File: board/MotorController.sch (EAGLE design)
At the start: 34 parts, among them Q1 IPP80P03P4L-04, Q2 8Mhz, T1 BT139X-600E, U1 ATTINY84-20PU

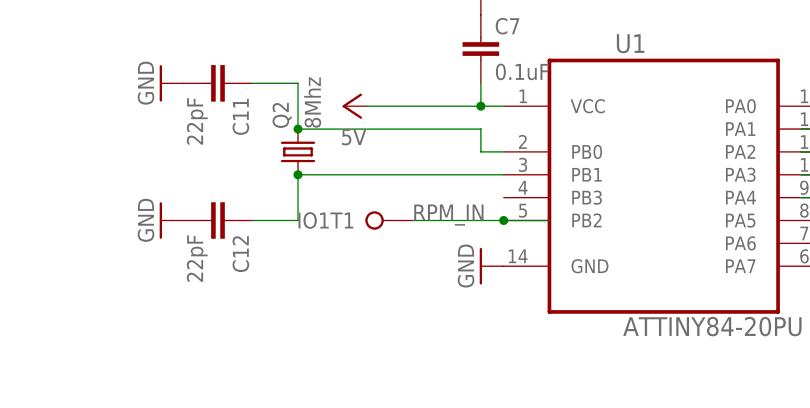
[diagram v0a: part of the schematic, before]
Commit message: Pull up reset line
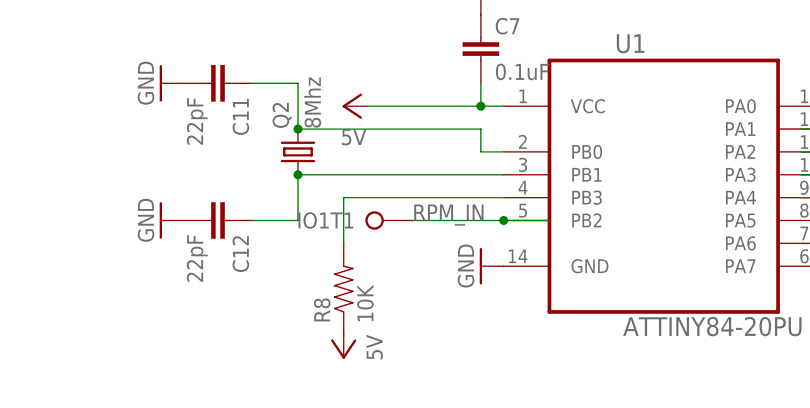
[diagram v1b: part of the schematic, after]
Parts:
- added R8: 10K, SaintGimp:RESISTOR-7.5MM
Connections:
- new net N$2: R8.2, U1.PB3
- new net VCC: R8.1
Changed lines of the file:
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@@
 <part name="5V1" library="SaintGimp" deviceset="VCC" device="" value="5V"/>
 <part name="5V2" library="SaintGimp" deviceset="VCC" device="" value="5V"/>
+<part name="R8" library="SaintGimp" deviceset="RESISTOR-*" device="7.5MM" value="10K"/>
+<part name="5V3" library="SaintGimp" deviceset="VCC" device="" value="5V"/>
 </parts>
 <sheets>
@@
 <instance part="5V1" gate="VCC" x="167.64" y="10.16"/>
 <instance part="5V2" gate="VCC" x="167.64" y="-20.32" rot="R180"/>
+<instance part="R8" gate="G$1" x="83.82" y="-12.7" rot="R90"/>
+<instance part="5V3" gate="VCC" x="83.82" y="-20.32" rot="R180"/>
 </instances>
 <busses>
@@
 </segment>
 </net>
+<net name="N$2" class="0">
+<segment>
+<pinref part="U1" gate="A" pin="PB3"/>
+<wire x1="101.6" y1="-2.54" x2="83.82" y2="-2.54" width="0.1524" layer="91"/>
+<wire x1="83.82" y1="-2.54" x2="83.82" y2="-7.62" width="0.1524" layer="91"/>
+<pinref part="R8" gate="G$1" pin="2"/>
+</segment>
+</net>
+<net name="VCC" class="0">
+<segment>
+<pinref part="R8" gate="G$1" pin="1"/>
+<pinref part="5V3" gate="VCC" pin="VCC"/>
+</segment>
+</net>

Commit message: New board layout
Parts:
- removed 5VDISP, 5VPOT: SCREW-TERM-2, SaintGimp:SCREW-TERM-2
- removed IO1, IO2, IO3: SCREW-TERM-3, SaintGimp:SCREW-TERM-3
- removed R7: 2.2K, SaintGimp:RESISTOR-7.5MM
- added C10: 0.1uF, SaintGimp:CAPACITOR-5MM
- added CNTRL: SCREW-TERM-2, SaintGimp:SCREW-TERM-2
- added DISP, MOTOR, RAMP, SPD: SCREW-TERM-3, SaintGimp:SCREW-TERM-3
- C11, C12: device SaintGimp:CAPACITOR-5MM -> SaintGimp:CAPACITOR-2.5MM
- C6: value 0.1uF -> 1uF
- F1: value FUSEBLANK_5X20MM -> 4A
- R1, R2: value 1K -> (none)
- R3, R8: value 10K -> (none)
- R4, R5: value 220 -> (none)
- R6: value 2.2K -> (none)
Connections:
- removed net 5V: 5VDISPT1.KL, 5VPOTT1.KL, C2.+, C3.1, C7.2, DC1.OUT, R6.2, R7.1, U1.VCC
- removed net I2C_SCL: IO2T2.KL, R6.1, U1.PA4
- removed net I2C_SDA: IO1T3.KL, R7.2, U1.PA6
- new net N$8: DISPT3.KL, R6.1
- new net SERIAL_TX: R6.2, U1.PA6
- net 24V-PROTECTED: now also C10.2
- net DIR_IN: now also CNTRLT1.KL; no longer IO3T1.KL
- net DIR_OUT: now also MOTORT3.KL; no longer IO1T2.KL
- net GND: now also C10.1, DISPT2.KL, RAMPT2.KL, SPDT2.KL; no longer 5VDISPT2.KL, 5VPOTT2.KL
- net N$10: now also MOTORT1.KL; no longer IO2T1.KL
- net RAMP_IN: now also RAMPT3.KL; no longer IO3T2.KL
- net RPM_IN: now also MOTORT2.KL; no longer IO1T1.KL
- net SPD_IN: now also SPDT3.KL; no longer IO3T3.KL
- net START_IN: now also CNTRLT2.KL; no longer IO2T3.KL
- net VCC: now also C2.+, C3.1, C7.2, DC1.OUT, DISPT1.KL, RAMPT1.KL, SPDT1.KL, U1.VCC
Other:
- moved on the sheet: 24VOUTT1, 24VOUTT2, C11, C12, C2, C3, C4, C6, C7, C8, C9, DC1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

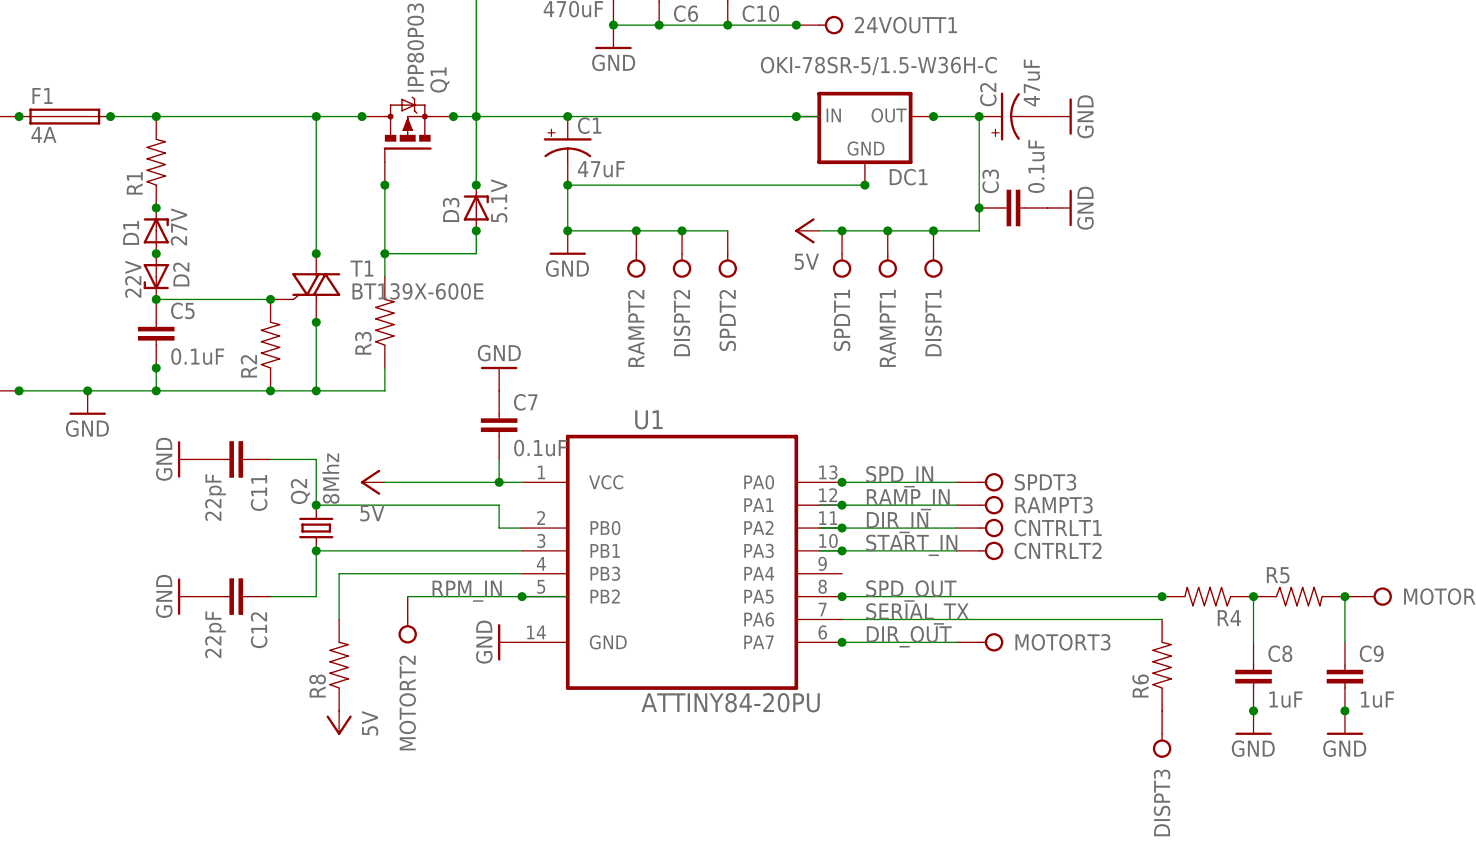
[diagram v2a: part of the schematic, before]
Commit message: Restore resistor values
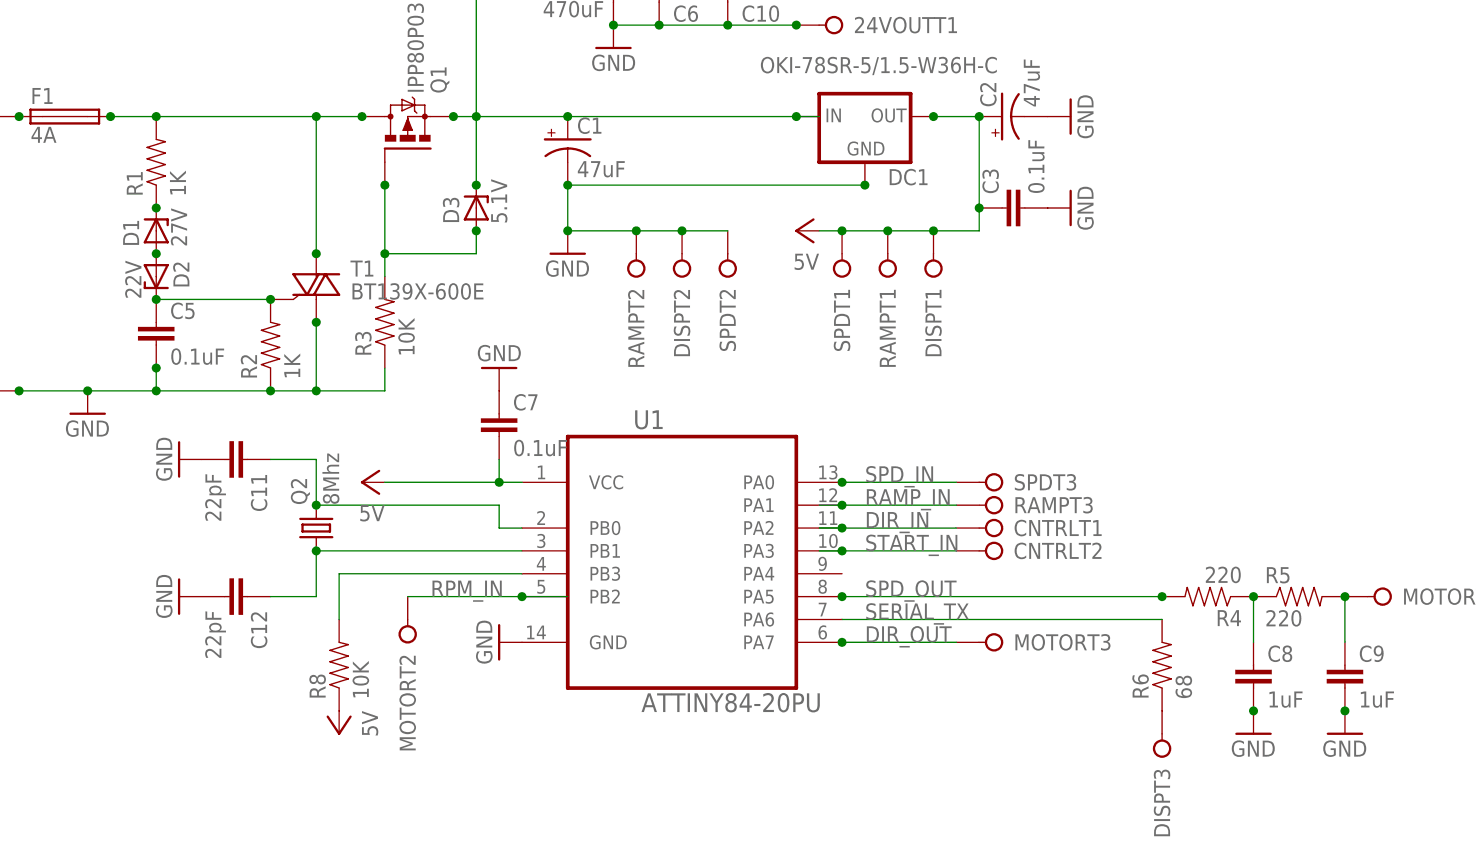
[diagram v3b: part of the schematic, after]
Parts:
- R1, R2: value (none) -> 1K
- R3, R8: value (none) -> 10K
- R4, R5: value (none) -> 220
- R6: value (none) -> 68
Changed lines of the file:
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@@
 <part name="D2" library="SaintGimp" deviceset="ZENER" device="-7.5" value="22V"/>
 <part name="D1" library="SaintGimp" deviceset="ZENER" device="-7.5" value="27V"/>
-<part name="R1" library="SaintGimp" deviceset="RESISTOR-*" device="7.5MM"/>
+<part name="R1" library="SaintGimp" deviceset="RESISTOR-*" device="7.5MM" value="1K"/>
 <part name="C5" library="SaintGimp" deviceset="CAPACITOR-*" device="5MM" value="0.1uF"/>
-<part name="R2" library="SaintGimp" deviceset="RESISTOR-*" device="7.5MM"/>
+<part name="R2" library="SaintGimp" deviceset="RESISTOR-*" device="7.5MM" value="1K"/>
 <part name="Q1" library="SaintGimp" deviceset="IPP80P03P4L-04" device="-H" value="IPP80P03P4L-04"/>
-<part name="R3" library="SaintGimp" deviceset="RESISTOR-*" device="7.5MM"/>
+<part name="R3" library="SaintGimp" deviceset="RESISTOR-*" device="7.5MM" value="10K"/>
 <part name="D3" library="SaintGimp" deviceset="ZENER" device="-7.5" value="5.1V"/>
 <part name="C2" library="SaintGimp" deviceset="CAP-POL" device="-2.5-5" value="47uF"/>
@@
 <part name="U1" library="SaintGimp" deviceset="ATTINY84-20PU" device=""/>
 <part name="C7" library="SaintGimp" deviceset="CAPACITOR-*" device="5MM" value="0.1uF"/>
-<part name="R4" library="SaintGimp" deviceset="RESISTOR-*" device="7.5MM"/>
-<part name="R5" library="SaintGimp" deviceset="RESISTOR-*" device="7.5MM"/>
+<part name="R4" library="SaintGimp" deviceset="RESISTOR-*" device="7.5MM" value="220"/>
+<part name="R5" library="SaintGimp" deviceset="RESISTOR-*" device="7.5MM" value="220"/>
 <part name="C8" library="SaintGimp" deviceset="CAPACITOR-*" device="5MM" value="1uF"/>
 <part name="GND7" library="SaintGimp" deviceset="GND" device=""/>
@@
 <part name="5V1" library="SaintGimp" deviceset="VCC" device="" value="5V"/>
 <part name="DC1" library="SaintGimp" deviceset="DC-CONV" device="" value="OKI-78SR-5/1.5-W36H-C"/>
-<part name="R8" library="SaintGimp" deviceset="RESISTOR-*" device="7.5MM"/>
+<part name="R8" library="SaintGimp" deviceset="RESISTOR-*" device="7.5MM" value="10K"/>
 <part name="5V3" library="SaintGimp" deviceset="VCC" device="" value="5V"/>
 <part name="C10" library="SaintGimp" deviceset="CAPACITOR-*" device="5MM" value="0.1uF"/>
-<part name="R6" library="SaintGimp" deviceset="RESISTOR-*" device="7.5MM"/>
+<part name="R6" library="SaintGimp" deviceset="RESISTOR-*" device="7.5MM" value="68"/>
 <part name="SPD" library="SaintGimp" deviceset="SCREW-TERM-3" device=""/>
 <part name="MOTOR" library="SaintGimp" deviceset="SCREW-TERM-3" device=""/>

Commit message: Board tweaks
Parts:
- removed C2: 47uF, SaintGimp:CAP-POL-2.5-5
- removed CNTRL: SCREW-TERM-2, SaintGimp:SCREW-TERM-2
- removed DISP, SPD: SCREW-TERM-3, SaintGimp:SCREW-TERM-3
- added FRONT: SCREW-TERM-5, SaintGimp:SCREW-TERM-5
- added MODE: SCREW-TERM-2, SaintGimp:SCREW-TERM-2
- C1: value 47uF -> 10uF; device SaintGimp:CAP-POL-2.5-5 -> SaintGimp:CAPACITOR-5MM
- C3: value 0.1uF -> 10uF
- MOTOR: value SCREW-TERM-3 -> SCREW-TERM-4; device SaintGimp:SCREW-TERM-3 -> SaintGimp:SCREW-TERM-4
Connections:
- net 24V-PROTECTED: now also C1.1; no longer C1.+
- net DIR_IN: now also MODET2.KL; no longer CNTRLT1.KL
- net GND: now also C1.2, FRONTT2.KL, MODET1.KL, MOTORT4.KL; no longer C1.-, C2.-, DISPT2.KL, SPDT2.KL
- net N$8: now also FRONTT3.KL; no longer DISPT3.KL
- net SPD_IN: now also FRONTT4.KL; no longer SPDT3.KL
- net START_IN: now also FRONTT5.KL; no longer CNTRLT2.KL
- net VCC: now also FRONTT1.KL; no longer C2.+, DISPT1.KL, SPDT1.KL
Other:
- moved on the sheet: C3
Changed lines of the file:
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@@
 <part name="24VOUT" library="SaintGimp" deviceset="SCREW-TERM-2" device=""/>
 <part name="RAMP" library="SaintGimp" deviceset="SCREW-TERM-3" device=""/>
-<part name="DISP" library="SaintGimp" deviceset="SCREW-TERM-3" device=""/>
-<part name="C1" library="SaintGimp" deviceset="CAP-POL" device="-2.5-5" value="47uF"/>
+<part name="FRONT" library="SaintGimp" deviceset="SCREW-TERM-5" device=""/>
 <part name="C4" library="SaintGimp" deviceset="CAP-POL" device="-25-14" value="470uF"/>
 <part name="F1" library="SaintGimp" deviceset="FUSE" device="" value="4A"/>
@@
 <part name="R3" library="SaintGimp" deviceset="RESISTOR-*" device="7.5MM" value="10K"/>
 <part name="D3" library="SaintGimp" deviceset="ZENER" device="-7.5" value="5.1V"/>
-<part name="C2" library="SaintGimp" deviceset="CAP-POL" device="-2.5-5" value="47uF"/>
-<part name="GND2" library="SaintGimp" deviceset="GND" device=""/>
-<part name="C3" library="SaintGimp" deviceset="CAPACITOR-*" device="5MM" value="0.1uF"/>
+<part name="C3" library="SaintGimp" deviceset="CAPACITOR-*" device="5MM" value="10uF"/>
 <part name="GND3" library="SaintGimp" deviceset="GND" device=""/>
 <part name="C6" library="SaintGimp" deviceset="CAPACITOR-*" device="5MM" value="1uF"/>
@@
 <part name="C10" library="SaintGimp" deviceset="CAPACITOR-*" device="5MM" value="0.1uF"/>
 <part name="R6" library="SaintGimp" deviceset="RESISTOR-*" device="7.5MM" value="68"/>
-<part name="SPD" library="SaintGimp" deviceset="SCREW-TERM-3" device=""/>
-<part name="MOTOR" library="SaintGimp" deviceset="SCREW-TERM-3" device=""/>
-<part name="CNTRL" library="SaintGimp" deviceset="SCREW-TERM-2" device=""/>
+<part name="MOTOR" library="SaintGimp" deviceset="SCREW-TERM-4" device=""/>
+<part name="MODE" library="SaintGimp" deviceset="SCREW-TERM-2" device=""/>
+<part name="C1" library="SaintGimp" deviceset="CAPACITOR-*" device="5MM" value="10uF"/>
 </parts>
 <sheets>
@@
 <instance part="RAMP" gate="T1" x="76.2" y="35.56" rot="R90"/>
 <instance part="RAMP" gate="T2" x="48.26" y="35.56" rot="R90"/>
-<instance part="DISP" gate="T1" x="81.28" y="35.56" rot="R90"/>
-<instance part="DISP" gate="T2" x="53.34" y="35.56" rot="R90"/>
-<instance part="C1" gate="G$1" x="40.64" y="50.8"/>
+<instance part="FRONT" gate="T1" x="81.28" y="35.56" rot="R90"/>
+<instance part="FRONT" gate="T2" x="53.34" y="35.56" rot="R90"/>
 <instance part="C4" gate="G$1" x="45.72" y="68.58" rot="MR0"/>
 <instance part="F1" gate="G$1" x="-15.24" y="53.34"/>
@@
 <instance part="R3" gate="G$1" x="20.32" y="30.48" rot="R90"/>
 <instance part="D3" gate="G$1" x="30.48" y="43.18" rot="R90"/>
-<instance part="C2" gate="G$1" x="88.9" y="53.34" rot="R90"/>
-<instance part="GND2" gate="1" x="96.52" y="53.34" rot="R90"/>
-<instance part="C3" gate="G$1" x="91.44" y="43.18" rot="R90"/>
-<instance part="GND3" gate="1" x="96.52" y="43.18" rot="R90"/>
+<instance part="C3" gate="G$1" x="91.44" y="48.26" rot="R90"/>
+<instance part="GND3" gate="1" x="96.52" y="48.26" rot="R90"/>
 <instance part="C6" gate="G$1" x="50.8" y="68.58" rot="MR180"/>
 <instance part="GND6" gate="1" x="33.02" y="-5.08" rot="R270"/>
@@
 <instance part="GND12" gate="1" x="-2.54" y="0" rot="R270"/>
 <instance part="5V2" gate="VCC" x="17.78" y="12.7" rot="R90"/>
-<instance part="5V1" gate="VCC" x="66.04" y="40.64" rot="R90"/>
+<instance part="5V1" gate="VCC" x="71.12" y="40.64" rot="R90"/>
 <instance part="DC1" gate="G$1" x="73.66" y="50.8" smashed="yes">
 <attribute name="NAME" x="76.2" y="45.72" size="1.778" layer="95"/>
@@
 <instance part="C10" gate="G$1" x="58.42" y="68.58" rot="MR180"/>
 <instance part="R6" gate="G$1" x="106.68" y="-7.62" rot="R90"/>
-<instance part="DISP" gate="T3" x="106.68" y="-17.78" rot="R90"/>
-<instance part="SPD" gate="T3" x="88.9" y="12.7" rot="R180"/>
-<instance part="SPD" gate="T1" x="71.12" y="35.56" rot="R90"/>
-<instance part="SPD" gate="T2" x="58.42" y="35.56" rot="R90"/>
+<instance part="FRONT" gate="T3" x="106.68" y="-17.78" rot="R90"/>
 <instance part="RAMP" gate="T3" x="88.9" y="10.16" rot="R180"/>
 <instance part="MOTOR" gate="T1" x="132.08" y="0" rot="R180"/>
-<instance part="CNTRL" gate="T2" x="88.9" y="5.08" rot="R180"/>
-<instance part="CNTRL" gate="T1" x="88.9" y="7.62" rot="R180"/>
 <instance part="MOTOR" gate="T2" x="22.86" y="-5.08" rot="R90"/>
 <instance part="MOTOR" gate="T3" x="88.9" y="-5.08" rot="R180"/>
+<instance part="FRONT" gate="T4" x="88.9" y="12.7" rot="R180"/>
+<instance part="FRONT" gate="T5" x="88.9" y="5.08" rot="R180"/>
+<instance part="MODE" gate="T2" x="88.9" y="7.62" rot="R180"/>
+<instance part="MODE" gate="T1" x="58.42" y="35.56" rot="R90"/>
+<instance part="MOTOR" gate="T4" x="63.5" y="35.56" rot="R90"/>
+<instance part="C1" gate="G$1" x="40.64" y="48.26"/>
 </instances>
 <busses>
@@
 <net name="GND" class="0">
 <segment>
-<pinref part="C1" gate="G$1" pin="-"/>
 <pinref part="GND1" gate="1" pin="GND"/>
 <wire x1="40.64" y1="40.64" x2="40.64" y2="45.72" width="0.1524" layer="91"/>
 <wire x1="73.66" y1="45.72" x2="40.64" y2="45.72" width="0.1524" layer="91"/>
-<junction x="40.64" y="45.72"/>
-<pinref part="DISP" gate="T2" pin="KL"/>
+<pinref part="FRONT" gate="T2" pin="KL"/>
 <pinref part="RAMP" gate="T2" pin="KL"/>
 <wire x1="53.34" y1="40.64" x2="48.26" y2="40.64" width="0.1524" layer="91"/>
@@
 <pinref part="DC1" gate="G$1" pin="GND"/>
 <junction x="73.66" y="45.72"/>
-<pinref part="SPD" gate="T2" pin="KL"/>
+<pinref part="MODE" gate="T1" pin="KL"/>
 <wire x1="58.42" y1="40.64" x2="53.34" y2="40.64" width="0.1524" layer="91"/>
 <junction x="53.34" y="40.64"/>
+<pinref part="MOTOR" gate="T4" pin="KL"/>
+<wire x1="63.5" y1="40.64" x2="58.42" y2="40.64" width="0.1524" layer="91"/>
+<junction x="58.42" y="40.64"/>
+<pinref part="C1" gate="G$1" pin="2"/>
+<junction x="40.64" y="45.72"/>
 </segment>
 <segment>
@@
 </segment>
 <segment>
-<pinref part="C2" gate="G$1" pin="-"/>
-<pinref part="GND2" gate="1" pin="GND"/>
-</segment>
-<segment>
 <pinref part="C3" gate="G$1" pin="2"/>
 <pinref part="GND3" gate="1" pin="GND"/>
@@
 <net name="24V-PROTECTED" class="1">
 <segment>
+<wire x1="30.48" y1="53.34" x2="40.64" y2="53.34" width="0.1524" layer="91"/>
 <wire x1="40.64" y1="53.34" x2="66.04" y2="53.34" width="0.1524" layer="91"/>
-<pinref part="C1" gate="G$1" pin="+"/>
 <wire x1="66.04" y1="53.34" x2="68.58" y2="53.34" width="0.1524" layer="91"/>
 <pinref part="Q1" gate="G$1" pin="S"/>
-<wire x1="40.64" y1="53.34" x2="30.48" y2="53.34" width="0.1524" layer="91"/>
-<junction x="40.64" y="53.34"/>
 <pinref part="D3" gate="G$1" pin="C"/>
 <wire x1="30.48" y1="53.34" x2="27.94" y2="53.34" width="0.1524" layer="91"/>
@@
 <junction x="45.72" y="71.12"/>
 <wire x1="30.48" y1="71.12" x2="30.48" y2="53.34" width="0.1524" layer="91"/>
+<pinref part="C1" gate="G$1" pin="1"/>
+<junction x="40.64" y="53.34"/>
 </segment>
 </net>
@@
 <wire x1="71.12" y1="5.08" x2="83.82" y2="5.08" width="0.1524" layer="91"/>
 <junction x="71.12" y="5.08"/>
-<pinref part="CNTRL" gate="T2" pin="KL"/>
+<pinref part="FRONT" gate="T5" pin="KL"/>
 </segment>
 </net>
@@
 <wire x1="83.82" y1="7.62" x2="71.12" y2="7.62" width="0.1524" layer="91"/>
 <junction x="71.12" y="7.62"/>
-<pinref part="CNTRL" gate="T1" pin="KL"/>
+<pinref part="MODE" gate="T2" pin="KL"/>
 </segment>
 </net>
@@
 <label x="73.66" y="12.7" size="1.778" layer="95"/>
 <junction x="71.12" y="12.7"/>
-<pinref part="SPD" gate="T3" pin="KL"/>
+<pinref part="FRONT" gate="T4" pin="KL"/>
 </segment>
 </net>
@@
 <segment>
 <pinref part="C3" gate="G$1" pin="1"/>
-<wire x1="86.36" y1="43.18" x2="86.36" y2="40.64" width="0.1524" layer="91"/>
+<wire x1="86.36" y1="48.26" x2="86.36" y2="40.64" width="0.1524" layer="91"/>
 <pinref part="RAMP" gate="T1" pin="KL"/>
-<pinref part="DISP" gate="T1" pin="KL"/>
+<pinref part="FRONT" gate="T1" pin="KL"/>
 <wire x1="81.28" y1="40.64" x2="76.2" y2="40.64" width="0.1524" layer="91"/>
 <junction x="76.2" y="40.64"/>
 <wire x1="86.36" y1="40.64" x2="81.28" y2="40.64" width="0.1524" layer="91"/>
 <junction x="81.28" y="40.64"/>
-<pinref part="C2" gate="G$1" pin="+"/>
-<wire x1="86.36" y1="43.18" x2="86.36" y2="53.34" width="0.1524" layer="91"/>
-<junction x="86.36" y="43.18"/>
+<wire x1="86.36" y1="48.26" x2="86.36" y2="53.34" width="0.1524" layer="91"/>
+<junction x="86.36" y="48.26"/>
 <pinref part="5V1" gate="VCC" pin="VCC"/>
-<wire x1="76.2" y1="40.64" x2="71.12" y2="40.64" width="0.1524" layer="91"/>
+<wire x1="76.2" y1="40.64" x2="73.66" y2="40.64" width="0.1524" layer="91"/>
 <pinref part="DC1" gate="G$1" pin="OUT"/>
-<wire x1="71.12" y1="40.64" x2="68.58" y2="40.64" width="0.1524" layer="91"/>
 <wire x1="86.36" y1="53.34" x2="81.28" y2="53.34" width="0.1524" layer="91"/>
-<junction x="86.36" y="53.34"/>
 <junction x="81.28" y="53.34"/>
-<pinref part="SPD" gate="T1" pin="KL"/>
-<junction x="71.12" y="40.64"/>
 </segment>
 </net>
@@
 <segment>
 <pinref part="R6" gate="G$1" pin="1"/>
-<pinref part="DISP" gate="T3" pin="KL"/>
-</segment>
-</net>
+<pinref part="FRONT" gate="T3" pin="KL"/>
+</segment>
+</net>
